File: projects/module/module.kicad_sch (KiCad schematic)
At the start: 18 parts, among them J1 Conn_01x08_Pin, Y1 Crystal_GND24

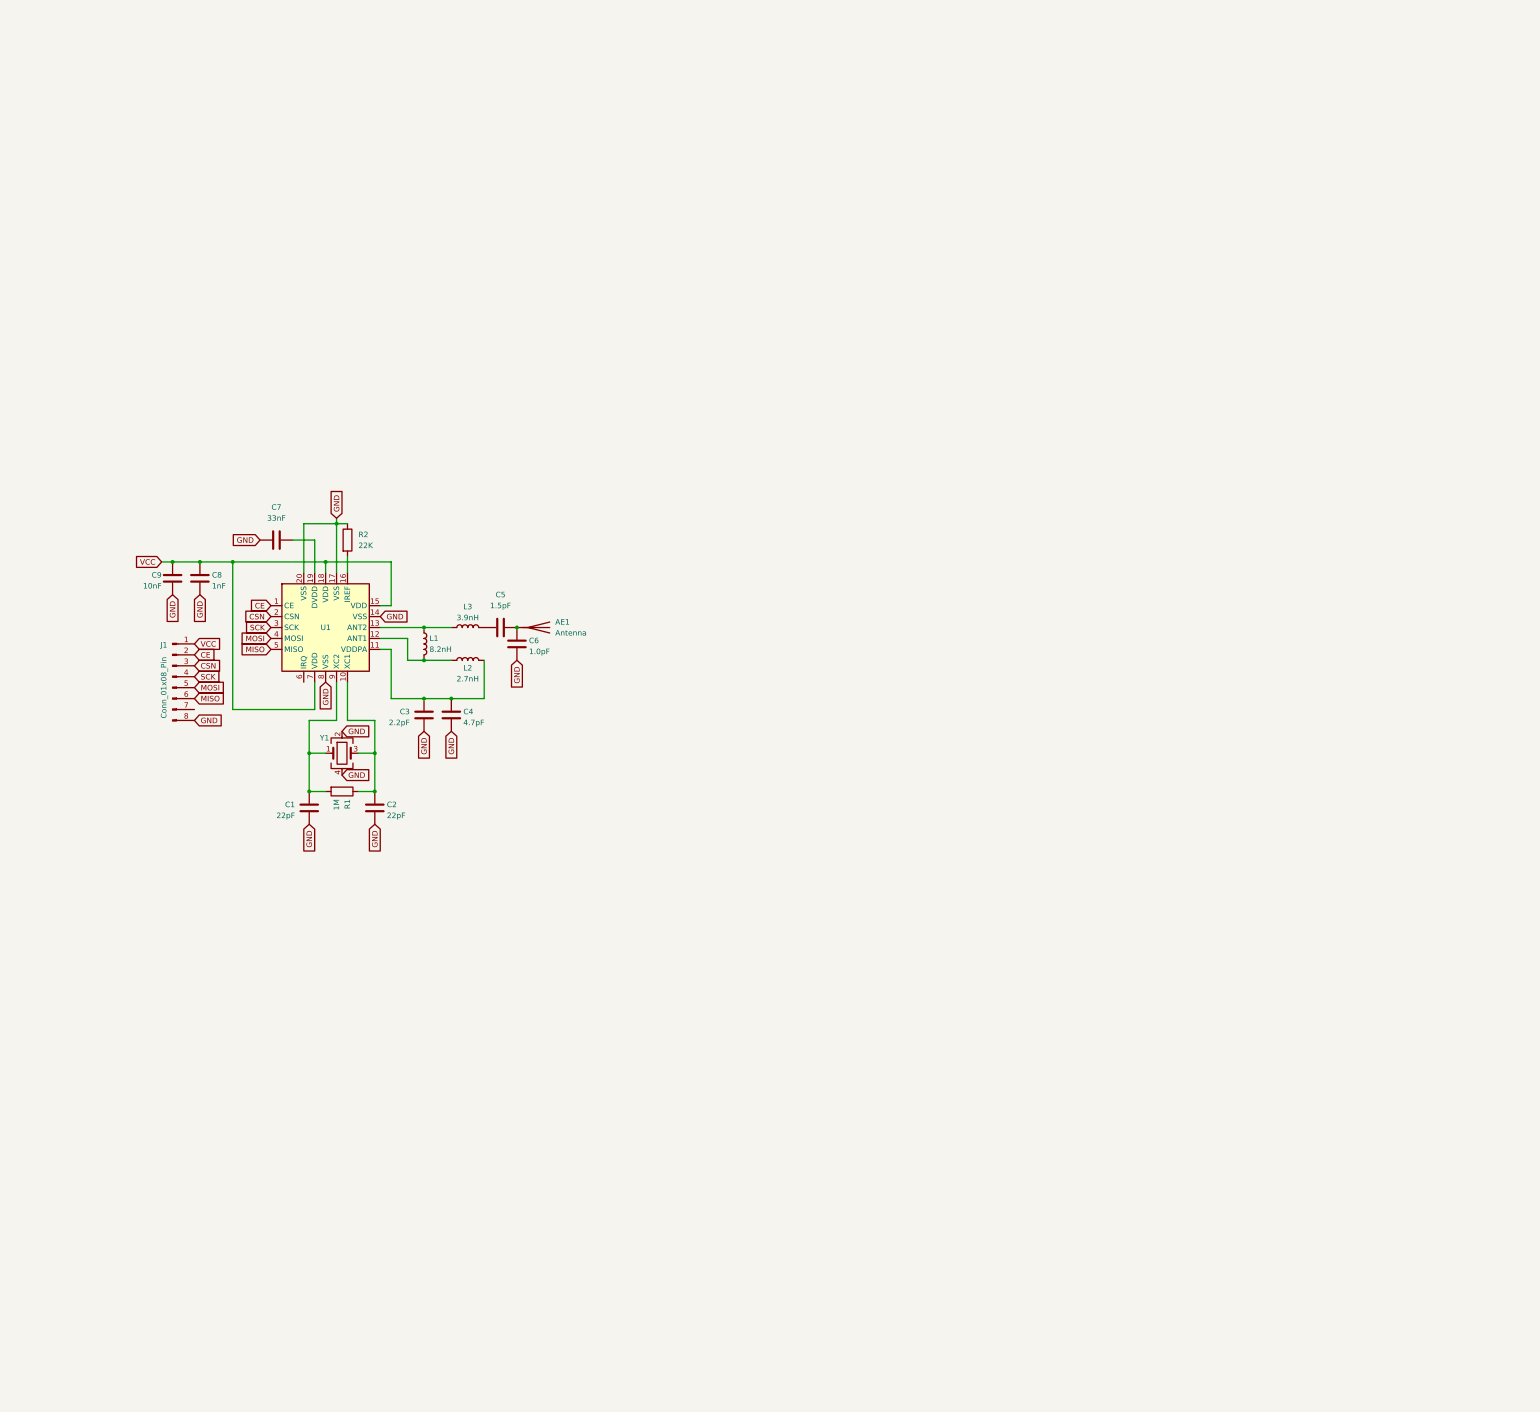
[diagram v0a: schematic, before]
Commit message: Added breakout module. Added custom thin header holes. Sunk USB-C
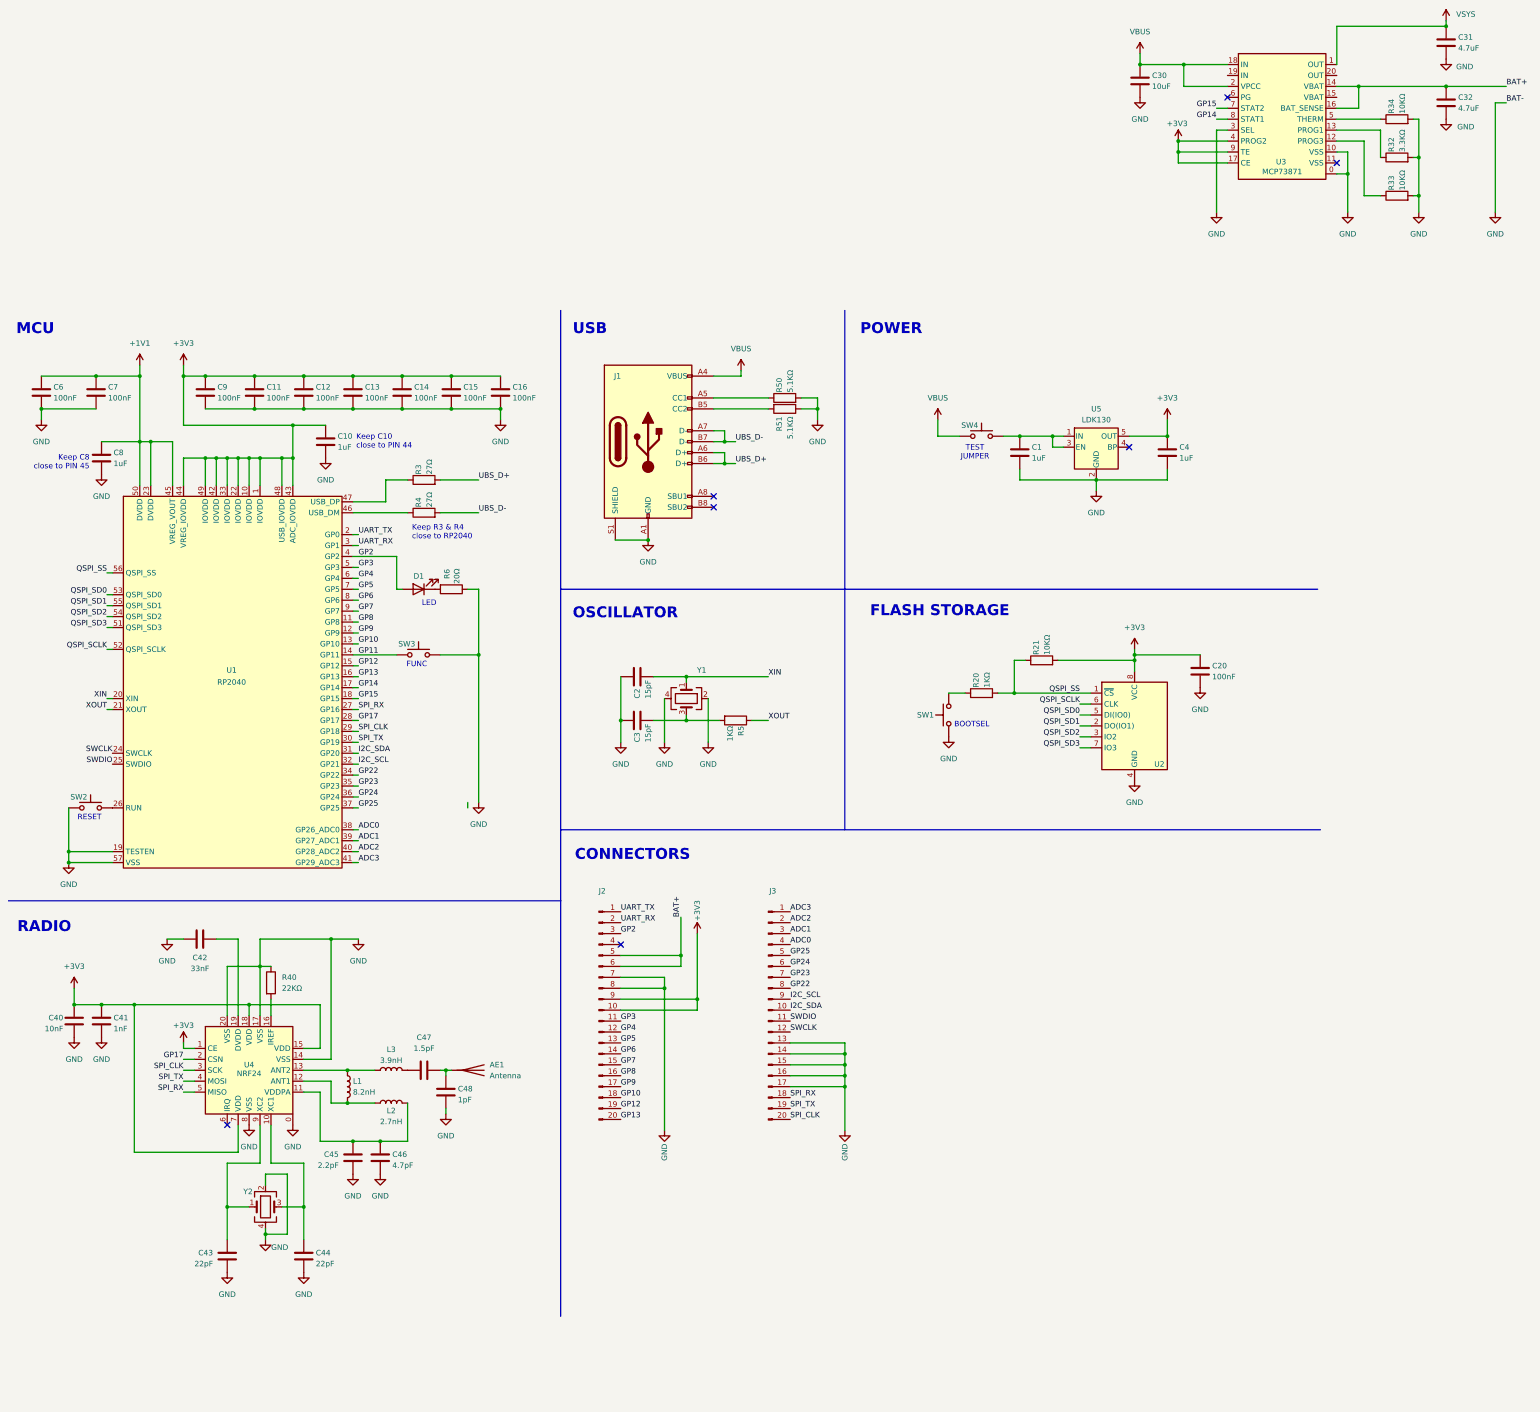
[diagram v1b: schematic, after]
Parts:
- removed J1: Conn_01x08_Pin, Connector_PinHeader_2.54mm:PinHeader_1x08_P2.54mm_Vertical, symbol Connector:Conn_01x08_Pin
- removed R1: 1M, ILO_fp:0402, symbol Device:R
- added C1, C10, C4, C8: 1uF, ILO_fp:0402_compact, symbol Device:C
- added C11, C12, C13, C14, C15, C16, C20, C6, C7, C9: 100nF, ILO_fp:0402_compact, symbol Device:C
- added C2, C3: 15pF, ILO_fp:0402_compact, symbol Device:C
- added C30: 10uF, symbol Device:C
- added C31, C32: 4.7uF, symbol Device:C
- added D1: Diode, ILO_fp:0603_d, symbol Device:LED
- added J1: USB_C, ILO_fp:USB_C2927298, symbol Connector:USB_C_Receptacle_USB2.0_16P
- added J2, J3: Conn_01x20_Pin, ILO_fp:Hirose_DF12NB, symbol Connector:Conn_01x20_Pin
- added R20, R5: 1KΩ, ILO_fp:0402_compact, symbol Device:R
- added R21: 10KΩ, ILO_fp:0402_compact, symbol Device:R
- added R3, R4: 27Ω, ILO_fp:0402_compact, symbol Device:R
- added R32: 3.3KΩ, symbol Device:R
- added R33, R34: 10KΩ, symbol Device:R
- added R50, R51: 5.1KΩ, ILO_fp:0402_compact, symbol Device:R
- added R6: 20Ω, ILO_fp:0603, symbol Device:R
- added SW1, SW2, SW3: SW_Push, ILO_fp:Alpsalpine_SKRP_compact, symbol Switch:SW_Push
- added SW4: SW_Push, ILO_fp:Header_2x_compact, symbol Switch:SW_Push
- added U1: RP2040, Package_DFN_QFN:QFN-56-1EP_7x7mm_P0.4mm_EP3.2x3.2mm, symbol ILO_sym:Raspberry_RP2040
- added U2: FLASH, ILO_fp:Winbond_W25Q, symbol Memory_Flash:W25Q128JVS
- added U3: MCP73871, symbol ILO_sym:Microchip_MCP73871
- added U5: LDK130, Package_TO_SOT_SMD:SOT-23-5, symbol Regulator_Linear:LDK130-33_SOT23_SOT353
- added Y1: 12MHz, Crystal:Crystal_SMD_2520-4Pin_2.5x2.0mm, symbol Device:Crystal_GND24
- C40: renamed from C9; footprint ILO_fp:0402 -> ILO_fp:0402_compact; LCSC C408912 -> C15195
- C41: renamed from C8; footprint ILO_fp:0402 -> ILO_fp:0402_compact; LCSC C327779 -> C1523
- C42: renamed from C7; footprint ILO_fp:0402 -> ILO_fp:0402_compact; LCSC C387932 -> C1585
- C43: renamed from C1; footprint ILO_fp:0402 -> ILO_fp:0402_compact; LCSC C327788 -> C1555
- C44: renamed from C2; footprint ILO_fp:0402 -> ILO_fp:0402_compact; LCSC C327788 -> C1555
- C45: renamed from C3; footprint ILO_fp:0402 -> ILO_fp:0402_compact; LCSC C338141 -> C1559
- C46: renamed from C4; footprint ILO_fp:0402 -> ILO_fp:0402_compact; LCSC C172823 -> C1569
- C47: renamed from C5; footprint ILO_fp:0402 -> ILO_fp:0402_compact; LCSC C880756 -> C1552
- C48: renamed from C6; value 1.0pF -> 1pF; footprint ILO_fp:0402 -> ILO_fp:0402_compact; LCSC C323585 -> C1550
- L1, L2, L3: footprint ILO_fp:0402 -> ILO_fp:0402_compact
- R40: renamed from R2; value 22K -> 22KΩ; footprint ILO_fp:0402 -> ILO_fp:0402_compact
- U4: renamed from U1; value ~ -> NRF24; footprint Package_DFN_QFN:QFN-20-1EP_4x4mm_P0.5mm_EP2.6x2.6mm -> ILO_fp:QFN20_internal_routing
- Y2: renamed from Y1; value Crystal_GND24 -> 16MHz
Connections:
- net VCC is gone; now on net +3V3: C40.1, C41.1, U4.15 (VDD), U4.18 (VDD), U4.7 (VDD)
- net GND: now also C42.2, U4.0, C1.1, C10.1, C11.1, C12.1, C13.1, C14.1, C15.1, C16.1, C2.2, C20.1, C3.2, C30.1, C31.1, C32.1, C4.1, C6.1, C7.1, C8.1, C9.1, J1.A1 (GND), J1.A12 (GND), J1.B1 (GND), J1.B12 (GND), J1.S1 (SHIELD), J2.7 (Pin_7), J2.8 (Pin_8), J3.13 (Pin_13), J3.14 (Pin_14), J3.15 (Pin_15), J3.16 (Pin_16), J3.17 (Pin_17), R32.2, R33.2, R34.2, R50.2, R51.1, R6.1, SW1.1, SW2.1, SW3.2, U1.19 (TESTEN), U1.57 (VSS), U2.4 (GND), U3.0, U3.10 (VSS), U3.3 (SEL), U5.2 (GND), Y1.2, Y1.4; no longer C42.1
- net at U4.19 (DVDD): now also C42.1; no longer C42.2
- net CE renamed +3V3
- net +3V3: now also C10.2, C11.2, C12.2, C13.2, C14.2, C15.2, C16.2, C20.2, C4.2, C9.2, J2.10 (Pin_10), J2.9 (Pin_9), R21.2, U1.1 (IOVDD), U1.10 (IOVDD), U1.22 (IOVDD), U1.33 (IOVDD), U1.42 (IOVDD), U1.43 (ADC_IOVDD), U1.44 (VREG_IOVDD), U1.48 (USB_IOVDD), U1.49 (IOVDD), U2.8 (VCC), U3.17 (CE), U3.4 (PROG2), U3.9 (TE), U5.5 (OUT)
- net CSN renamed GP17
- net GP17: now also U1.28 (GP17)
- net MISO renamed SPI_RX
- net SPI_RX: now also J3.18 (Pin_18), U1.27 (GP16)
- net MOSI renamed SPI_TX
- net SPI_TX: now also J3.19 (Pin_19), U1.30 (GP19)
- net SCK renamed SPI_CLK
- net SPI_CLK: now also J3.20 (Pin_20), U1.29 (GP18)
- new net: R34.1, U3.5 (THERM)
- new net: C3.1, R5.2, Y1.3
- new net: SW2.2, U1.26 (RUN)
- new net: R4.1, U1.46 (USB_DM)
- new net: R3.1, U1.47 (USB_DP)
- new net: R20.1, SW1.2
- new net: R33.1, U3.12 (PROG3)
- new net: R32.1, U3.13 (PROG1)
- new net: D1.1 (K), R6.2
- new net: J1.A5 (CC1), R50.1
- new net: J1.B5 (CC2), R51.2
- new net: C1.2, SW4.2, U5.1 (IN), U5.3 (EN)
- new net +1V1: C6.2, C7.2, C8.2, U1.23 (DVDD), U1.45 (VREG_VOUT), U1.50 (DVDD)
- new net ADC0: J3.4 (Pin_4), U1.38 (GP26_ADC0)
- new net ADC1: J3.3 (Pin_3), U1.39 (GP27_ADC1)
- new net ADC2: J3.2 (Pin_2), U1.40 (GP28_ADC2)
- new net ADC3: J3.1 (Pin_1), U1.41 (GP29_ADC3)
- new net BAT+: C32.2, J2.5 (Pin_5), J2.6 (Pin_6), U3.14 (VBAT), U3.16 (BAT_SENSE)
- new net GP10: J2.18 (Pin_18), U1.13 (GP10)
- new net GP11: SW3.1, U1.14 (GP11)
- new net GP12: J2.19 (Pin_19), U1.15 (GP12)
- new net GP13: J2.20 (Pin_20), U1.16 (GP13)
- new net GP14: U1.17 (GP14), U3.8 (STAT1)
- new net GP15: U1.18 (GP15), U3.7 (STAT2)
- new net GP2: D1.2 (A), J2.3 (Pin_3), U1.4 (GP2)
- new net GP22: J3.8 (Pin_8), U1.34 (GP22)
- new net GP23: J3.7 (Pin_7), U1.35 (GP23)
- new net GP24: J3.6 (Pin_6), U1.36 (GP24)
- new net GP25: J3.5 (Pin_5), U1.37 (GP25)
- new net GP3: J2.11 (Pin_11), U1.5 (GP3)
- new net GP4: J2.12 (Pin_12), U1.6 (GP4)
- new net GP5: J2.13 (Pin_13), U1.7 (GP5)
- new net GP6: J2.14 (Pin_14), U1.8 (GP6)
- new net GP7: J2.15 (Pin_15), U1.9 (GP7)
- new net GP8: J2.16 (Pin_16), U1.11 (GP8)
- new net GP9: J2.17 (Pin_17), U1.12 (GP9)
- new net I2C_SCL: J3.9 (Pin_9), U1.32 (GP21)
- new net I2C_SDA: J3.10 (Pin_10), U1.31 (GP20)
- new net QSPI_SCLK: U1.52 (QSPI_SCLK), U2.6 (CLK)
- new net QSPI_SD0: U1.53 (QSPI_SD0), U2.5 (DI(IO0))
- new net QSPI_SD1: U1.55 (QSPI_SD1), U2.2 (DO(IO1))
- new net QSPI_SD2: U1.54 (QSPI_SD2), U2.3 (IO2)
- new net QSPI_SD3: U1.51 (QSPI_SD3), U2.7 (IO3)
- new net QSPI_SS: R20.2, R21.1, U1.56 (QSPI_SS), U2.1 (~{CS})
- new net SWCLK: J3.12 (Pin_12), U1.24 (SWCLK)
- new net SWDIO: J3.11 (Pin_11), U1.25 (SWDIO)
- new net UART_RX: J2.2 (Pin_2), U1.3 (GP1)
- new net UART_TX: J2.1 (Pin_1), U1.2 (GP0)
- new net UBS_D+: J1.A6 (D+), J1.B6 (D+), R3.2
- new net UBS_D-: J1.A7 (D-), J1.B7 (D-), R4.2
- new net VBUS: C30.2, J1.A4 (VBUS), J1.A9 (VBUS), J1.B4 (VBUS), J1.B9 (VBUS), SW4.1, U3.18 (IN), U3.2 (VPCC)
- new net VSYS: C31.2, U3.1 (OUT)
- new net XIN: C2.1, U1.20 (XIN), Y1.1
- new net XOUT: R5.1, U1.21 (XOUT)
- no-connect marks 0 -> 7
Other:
- note added: "BOOTSEL"
- note added: "CONNECTORS"
- note added: "FLASH STORAGE"
- note added: "FUNC"
- note added: "Keep C10 close to PIN 44"
- note added: "Keep C8 close to PIN 45"
- note added: "Keep R3 & R4 close to RP2040"
- note added: "LED"
- note added: "MCU"
- note added: "OSCILLATOR"
- note added: "POWER"
- note added: "RADIO"
- note added: "RESET"
- note added: "TEST JUMPER"
- note added: "USB"
- moved on the sheet: AE1, C40, C41, C42, C43, C44, C45, C46, C47, C48, L1, L2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

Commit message: RF module test 4
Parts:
- removed C31: 4.7uF, symbol Device:C
- removed SW2, SW3: SW_Push, ILO_fp:Alpsalpine_SKRP_compact, symbol Switch:SW_Push
- removed SW4: SW_Push, ILO_fp:Header_2x_compact, symbol Switch:SW_Push
- added J4, J5: Conn_01x01_Pin, ILO_fp:Pad_1mm, symbol Connector:Conn_01x01_Pin
- C30: footprint (none) -> ILO_fp:0402_compact; Export (none) -> yes; LCSC (none) -> C15525; Mount (none) -> SMD
- C32: footprint (none) -> ILO_fp:0402_compact; Export (none) -> yes; LCSC (none) -> C23733; Mount (none) -> SMD
- C57: renamed from C42; LCSC C1585 -> C301939
- J1: footprint ILO_fp:USB_C2927298 -> ILO_fp:USB_C3019717; Group Connector -> USB; LCSC C2927298 -> C3019717
- R32: footprint (none) -> ILO_fp:0402_compact; Export (none) -> yes; LCSC (none) -> C137992; Mount (none) -> SMD
- R33, R34: footprint (none) -> ILO_fp:0402_compact; LCSC (none) -> C25744
- U3: footprint (none) -> ILO_fp:QFN20_internal_routing; Export (none) -> yes; Group (none) -> Power IC; LCSC (none) -> C511310; Mount (none) -> SMD
- renumbered C1 to C41, C4 to C42, C43 to C51, C44 to C52, C45 to C53, C46 to C54, C47 to C55, C48 to C56, C41 to C58, C40 to C59, R40 to R52, U5 to U4, U4 to U5
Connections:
- net +3V3: no longer U3.17 (CE), U3.4 (PROG2), U3.9 (TE)
- net GND: now also J2.3 (Pin_3), J2.4 (Pin_4), J3.11 (Pin_11), J3.12 (Pin_12); no longer J3.17 (Pin_17)
- net GP10: now also J2.17 (Pin_17); no longer J2.18 (Pin_18)
- net GP11: now also J2.18 (Pin_18)
- net GP14: now also U3.7 (STAT2); no longer U3.8 (STAT1)
- net GP15: now also U3.8 (STAT1); no longer U3.7 (STAT2)
- net GP2: now also R20.1, SW1.2; no longer D1.2 (A), J2.3 (Pin_3)
- net GP3: now also D1.2 (A); no longer J2.11 (Pin_11)
- net GP4: now also J2.11 (Pin_11); no longer J2.12 (Pin_12)
- net GP5: now also J2.12 (Pin_12); no longer J2.13 (Pin_13)
- net GP6: now also J2.13 (Pin_13); no longer J2.14 (Pin_14)
- net GP7: now also J2.14 (Pin_14); no longer J2.15 (Pin_15)
- net GP8: now also J2.15 (Pin_15); no longer J2.16 (Pin_16)
- net GP9: now also J2.16 (Pin_16); no longer J2.17 (Pin_17)
- net SWCLK: no longer J3.12 (Pin_12)
- net SWDIO: no longer J3.11 (Pin_11)
- net VBUS: now also U3.19 (IN), J4.1 (Pin_1)
- net VSYS: now also C41.2, U3.17 (CE), U3.20 (OUT), U3.4 (PROG2), U3.9 (TE), U4.1 (IN), U4.3 (EN), J5.1 (Pin_1)
- net RUN: now reaches U1.26 (RUN)
- net RUN: now also J3.17 (Pin_17)
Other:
- note added: "CLOCK"
- note removed: "OSCILLATOR"
- note removed: "RESET"
- note removed: "TEST JUMPER"
- moved on the sheet: AE1, C2, C20, C3, C30, C32, C41, C42, C51, C52, C53, C54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

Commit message: RF module test 5
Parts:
- removed J4, J5: Conn_01x01_Pin, ILO_fp:Pad_1mm, symbol Connector:Conn_01x01_Pin
- renumbered R50 to R40, R51 to R41
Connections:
- net I2C_SCL renamed GP21
- net I2C_SDA renamed GP20
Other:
- moved on the sheet: AE1, C51, C52, C53, C54, C55, C56, C57, C58, C59, L1, L2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

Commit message: RF module test 6
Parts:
- AE1: footprint Diode_SMD:D_1206_3216Metric -> ILO_fp:Yageo_ANT3216
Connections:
- net BAT+: now also U3.15 (VBAT)
- net GND: now also U3.11 (VSS)
- no-connect marks 7 -> 5
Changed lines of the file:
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@@
 	)
 	(junction
+		(at 265.43 53.34)
+		(diameter 0)
+		(color 0 0 0 0)
+	)
+	(junction
 		(at 176.53 191.77)
 		(diameter 0)
@@
 	)
 	(junction
+		(at 262.89 68.58)
+		(diameter 0)
+		(color 0 0 0 0)
+	)
+	(junction
 		(at 69.85 27.94)
 		(diameter 0)
@@
 	)
 	(no_connect
-		(at 260.35 53.34)
-	)
-	(no_connect
 		(at 176.53 58.42)
 	)
 	(no_connect
-		(at 260.35 68.58)
-	)
-	(no_connect
 		(at 293.37 30.48)
 	)
@@
 	(wire
 		(pts
-			(xy 265.43 55.88) (xy 265.43 50.8)
+			(xy 265.43 55.88) (xy 265.43 53.34)
 		)
 		(stroke
@@
 	(wire
 		(pts
+			(xy 265.43 53.34) (xy 265.43 50.8)
+		)
+		(stroke
+			(width 0)
+			(type default)
+		)
+	)
+	(wire
+		(pts
 			(xy 279.4 76.2) (xy 278.13 76.2)
 		)
@@
 	(wire
 		(pts
+			(xy 260.35 53.34) (xy 265.43 53.34)
+		)
+		(stroke
+			(width 0)
+			(type default)
+		)
+	)
+	(wire
+		(pts
 			(xy 113.03 52.07) (xy 121.92 52.07)
 		)
@@
 	(wire
 		(pts
+			(xy 260.35 68.58) (xy 262.89 68.58)
+		)
+		(stroke
+			(width 0)
+			(type default)
+		)
+	)
+	(wire
+		(pts
 			(xy 115.57 27.94) (xy 127 27.94)
 		)
@@
 	(wire
 		(pts
-			(xy 262.89 66.04) (xy 262.89 71.12)
+			(xy 262.89 66.04) (xy 262.89 68.58)
 		)
 		(stroke
@@
 	(wire
 		(pts
+			(xy 262.89 68.58) (xy 262.89 71.12)
+		)
+		(stroke
+			(width 0)
+			(type default)
+		)
+	)
+	(wire
+		(pts
 			(xy 91.44 204.47) (xy 97.79 204.47)
 		)
@@
 			)
 		)
-		(property "Footprint" "Diode_SMD:D_1206_3216Metric"
+		(property "Footprint" "ILO_fp:Yageo_ANT3216"
 			(at 120.65 196.85 0)
 			(effects

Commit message: RF module test 7.5
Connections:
- net GP20 renamed UART1_TX
- net GP21 renamed UART1_RX
- net GP22 renamed I2C_SDA
- net GP23 renamed I2C_SCL
- net UART_RX renamed UART0_RX
- net UART_TX renamed UART0_TX
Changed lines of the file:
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@@
 		)
 	)
-	(label "GP23"
+	(label "I2C_SCL"
 		(at 205.74 186.69 0)
 		(fields_autoplaced yes)
@@
 		)
 	)
-	(label "GP20"
+	(label "UART1_TX"
 		(at 205.74 194.31 0)
 		(fields_autoplaced yes)
@@
 		)
 	)
-	(label "GP23"
+	(label "I2C_SCL"
 		(at 93.98 123.19 0)
 		(fields_autoplaced yes)
@@
 		)
 	)
-	(label "GP20"
+	(label "UART1_TX"
 		(at 93.98 115.57 0)
 		(fields_autoplaced yes)
@@
 		)
 	)
-	(label "GP21"
+	(label "UART1_RX"
 		(at 205.74 191.77 0)
 		(fields_autoplaced yes)
@@
 		)
 	)
-	(label "UART_RX"
+	(label "UART0_RX"
 		(at 93.98 67.31 0)
 		(fields_autoplaced yes)
@@
 		)
 	)
-	(label "GP21"
+	(label "UART1_RX"
 		(at 93.98 118.11 0)
 		(fields_autoplaced yes)
@@
 		)
 	)
-	(label "GP22"
+	(label "I2C_SDA"
 		(at 93.98 120.65 0)
 		(fields_autoplaced yes)
@@
 		)
 	)
-	(label "UART_TX"
+	(label "UART0_TX"
 		(at 158.75 171.45 0)
 		(fields_autoplaced yes)
@@
 		)
 	)
-	(label "GP22"
+	(label "I2C_SDA"
 		(at 205.74 189.23 0)
 		(fields_autoplaced yes)
@@
 		)
 	)
-	(label "UART_TX"
+	(label "UART0_TX"
 		(at 93.98 64.77 0)
 		(fields_autoplaced yes)
@@
 		)
 	)
-	(label "UART_RX"
+	(label "UART0_RX"
 		(at 158.75 173.99 0)
 		(fields_autoplaced yes)
